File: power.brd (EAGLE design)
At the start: 25.4 x 25.4 mm, 7 parts

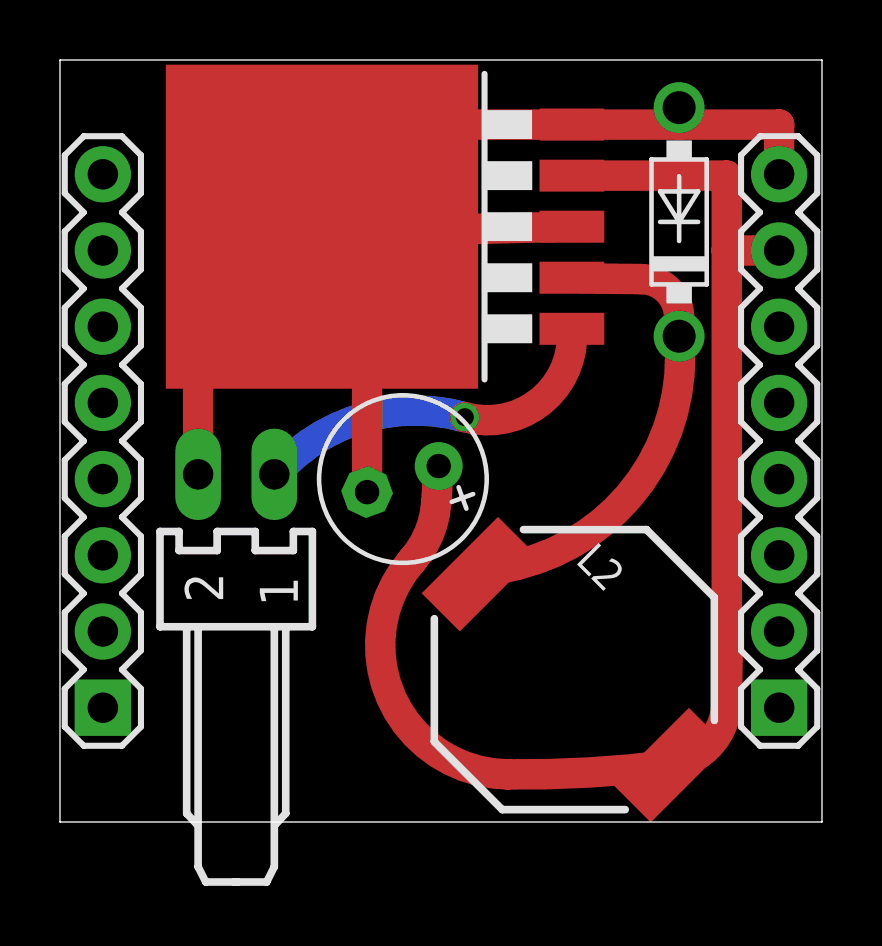
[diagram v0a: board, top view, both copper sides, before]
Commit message: Tidy up schematic and part numbers
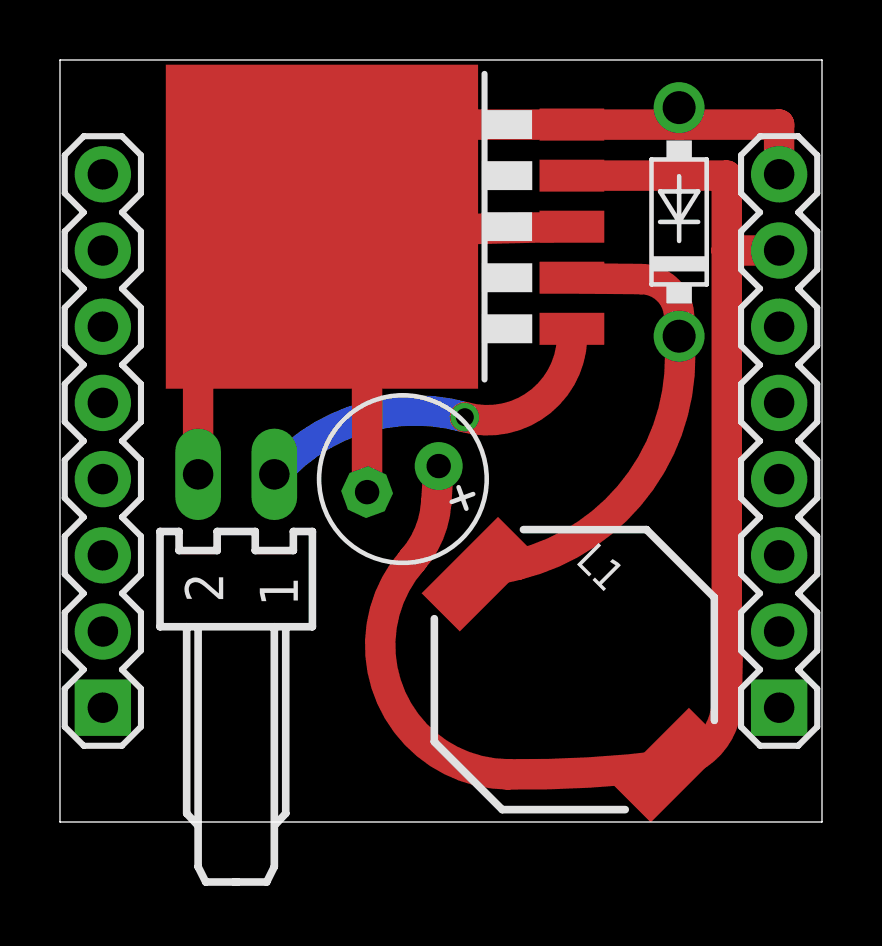
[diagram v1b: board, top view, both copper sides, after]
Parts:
- renumbered IC2 to IC1, L2 to L1
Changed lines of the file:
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@@
 <attribute name="VALUE" x="27.14625" y="2.54" size="1.27" layer="27" rot="R90"/>
 </element>
-<element name="IC2" library="linear" package="TO263-5" value="" x="11.27125" y="19.84375" smashed="yes" rot="R90">
+<element name="IC1" library="linear" package="TO263-5" value="" x="11.27125" y="19.84375" smashed="yes" rot="R90">
 <attribute name="VALUE" x="16.85925" y="26.70175" size="1.27" layer="27" rot="R180"/>
 </element>
@@
 <attribute name="OC_FARNELL" value="9731601" x="-51.91125" y="-9.8425" size="1.778" layer="27" display="off"/>
 </element>
-<element name="L2" library="SparkFun-Passives" package="SRU1038" value="" x="17.145" y="5.08" rot="R315"/>
+<element name="L1" library="SparkFun-Passives" package="SRU1038" value="" x="17.145" y="5.08" rot="R315"/>
 </elements>
 <signals>
@@
 <contactref element="C1" pad="-"/>
 <contactref element="PWR" pad="2"/>
-<contactref element="IC2" pad="3"/>
-<contactref element="IC2" pad="6"/>
-<contactref element="IC2" pad="5"/>
+<contactref element="IC1" pad="3"/>
+<contactref element="IC1" pad="6"/>
+<contactref element="IC1" pad="5"/>
 <wire x1="10.2365875" y1="10.995634375" x2="10.2365875" y2="19.685" width="1.016" layer="1"/>
 <wire x1="10.2365875" y1="19.685" x2="10.2365875" y2="19.84375" width="1.016" layer="1"/>
@@
 <contactref element="JP1" pad="7"/>
 <contactref element="C1" pad="+"/>
-<contactref element="IC2" pad="4"/>
-<contactref element="L2" pad="2"/>
+<contactref element="IC1" pad="4"/>
+<contactref element="L1" pad="2"/>
 <wire x1="17.06245" y1="21.54555" x2="22.225" y2="21.54555" width="1.016" layer="1"/>
 <wire x1="12.623409375" y1="11.8643625" x2="12.54125" y2="10.63625" width="1.016" layer="1"/>
@@
 </signal>
 <signal name="V+">
-<contactref element="IC2" pad="1"/>
+<contactref element="IC1" pad="1"/>
 <contactref element="PWR" pad="1"/>
 <wire x1="7.14375" y1="11.58875" x2="7.46125" y2="11.90625" width="1.016" layer="16"/>
@@
 </signal>
 <signal name="VOUT">
-<contactref element="IC2" pad="2"/>
+<contactref element="IC1" pad="2"/>
 <contactref element="D1" pad="C"/>
-<contactref element="L2" pad="1"/>
+<contactref element="L1" pad="1"/>
 <wire x1="20.6375" y1="16.1925" x2="20.6375" y2="16.8275" width="1.016" layer="1"/>
 <wire x1="20.6375" y1="16.8275" x2="19.3675" y2="18.0975" width="1.016" layer="1" curve="90"/>

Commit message: Bits on power
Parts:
- C1: value 680uf -> 220uf
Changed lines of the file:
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@@
 </element>
 <element name="D1" library="diode" package="DO41-7.6" value="1N5824" x="20.6375" y="20.0025" smashed="yes" rot="R90"/>
-<element name="C1" library="rcl" package="E2,5-6" value="680uf" x="11.43" y="11.43" smashed="yes" rot="R200"/>
+<element name="C1" library="rcl" package="E2,5-6" value="220uf" x="11.43" y="11.43" smashed="yes" rot="R200"/>
 <element name="PWR" library="con-molex" package="7395-02" value="22-05-7028-02" x="5.87375" y="11.58875" smashed="yes">
 <attribute name="OC_NEWARK" value="unknown" x="-51.91125" y="-9.8425" size="1.778" layer="27" display="off"/>
